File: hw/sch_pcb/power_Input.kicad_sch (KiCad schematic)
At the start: 40 parts, among them J1 USBC_USB4105-GF-A, J6 HEADER_2x01_PARALLEL, J7 HEADER_2x01_PARALLEL, J8 CONN1_1, J9 CONN1_1, Q1 DMTH3002LPS, U1 BQ25792RQMR1

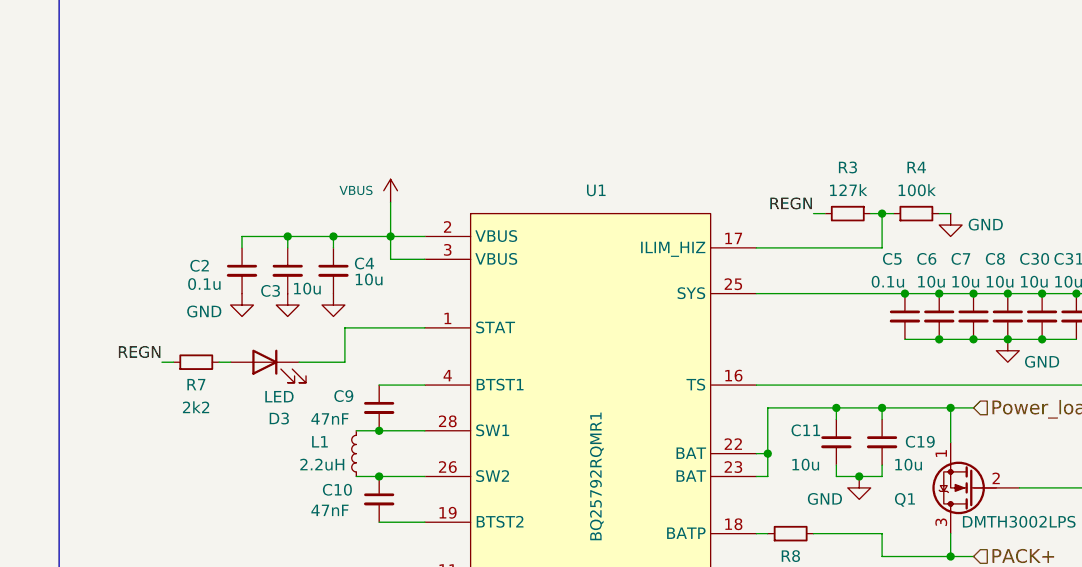
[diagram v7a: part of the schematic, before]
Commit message: Update USTids.
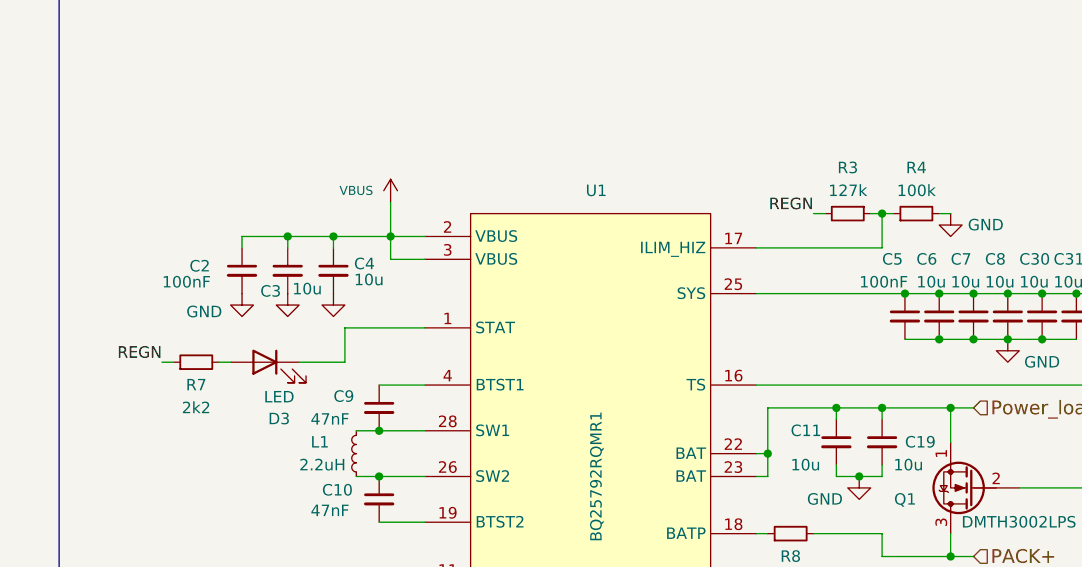
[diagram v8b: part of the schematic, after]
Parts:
- C10, C9: UST_ID (none) -> 65482046462c6d9e72056b98
- C11, C19, C25, C26, C27, C3, C30, C31, C4, C6, C7, C8: UST_ID (none) -> 5c70984712875079b91f8b53
- C2: value 0.1u -> 100nF; UST_ID (none) -> 5c70984712875079b91f8b4c
- C24: UST_ID (none) -> 5c70984812875079b91f8bf2
- C29: UST_ID 5c70984712875079b91f8b45 -> 5c70984712875079b91f8b4c
- C5: value 0.1u -> 100nF; UST_ID (none) -> 5c70984812875079b91f8bf2
- D3: UST_ID (none) -> 5c70984412875079b91f8892
- R11: UST_ID (none) -> 5c70984612875079b91f899f
- R3: UST_ID (none) -> 66a1559d6fdfe6f54e2ebeaa
- R4: UST_ID (none) -> 639ed3d540d28a66c9e88a9e
- R5: UST_ID (none) -> 66a159d36fdfe6f54e2ebef5
- R6: UST_ID (none) -> 66a15a4a6fdfe6f54e2ebf1b
- R7: UST_ID (none) -> 5c70984612875079b91f8990
- R8: UST_ID (none) -> 5c70984512875079b91f8977
- R9: UST_ID (none) -> 5c70984612875079b91f899c
- U1: UST_ID (none) -> 66a15cdb6fdfe6f54e2ebf66
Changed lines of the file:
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@@
 			)
 		)
+		(property "UST_ID" "66a1559d6fdfe6f54e2ebeaa"
+			(at 222.25 59.69 0)
+			(effects
+				(font
+					(size 1.27 1.27)
+				)
+				(hide yes)
+			)
+		)
 		(pin "1"
 		)
@@
 			)
 		)
+		(property "UST_ID" "5c70984712875079b91f8b53"
+			(at 247.65 71.12 0)
+			(effects
+				(font
+					(size 1.27 1.27)
+				)
+				(hide yes)
+			)
+		)
 		(pin "1"
 		)
@@
 			)
 		)
+		(property "UST_ID" "5c70984712875079b91f8b53"
+			(at 232.41 71.12 0)
+			(effects
+				(font
+					(size 1.27 1.27)
+				)
+				(hide yes)
+			)
+		)
 		(pin "1"
 		)
@@
 			)
 		)
+		(property "UST_ID" "5c70984412875079b91f8892"
+			(at 157.48 76.2 0)
+			(effects
+				(font
+					(size 1.27 1.27)
+				)
+				(hide yes)
+			)
+		)
 		(pin "1"
 		)
@@
 			)
 		)
+		(property "UST_ID" "5c70984712875079b91f8b53"
+			(at 160.02 66.04 0)
+			(effects
+				(font
+					(size 1.27 1.27)
+				)
+				(hide yes)
+			)
+		)
 		(pin "1"
 		)
@@
 			)
 		)
+		(property "UST_ID" "5c70984712875079b91f8b53"
+			(at 218.44 123.19 0)
+			(effects
+				(font
+					(size 1.27 1.27)
+				)
+				(hide yes)
+			)
+		)
 		(pin "1"
 		)
@@
 			)
 		)
-		(property "UST_ID" ""
+		(property "UST_ID" "5c70984612875079b91f899c"
 			(at 227.33 109.22 0)
 			(effects
@@
 			)
 		)
+		(property "UST_ID" "5c70984712875079b91f8b53"
+			(at 226.06 85.09 0)
+			(effects
+				(font
+					(size 1.27 1.27)
+				)
+				(hide yes)
+			)
+		)
 		(pin "1"
 		)
@@
 			)
 		)
+		(property "UST_ID" "66a15a4a6fdfe6f54e2ebf1b"
+			(at 256.54 82.55 0)
+			(effects
+				(font
+					(size 1.27 1.27)
+				)
+				(hide yes)
+			)
+		)
 		(pin "1"
 		)
@@
 			)
 		)
+		(property "UST_ID" "65482046462c6d9e72056b98"
+			(at 170.18 81.28 0)
+			(effects
+				(font
+					(size 1.27 1.27)
+				)
+				(hide yes)
+			)
+		)
 		(pin "1"
 		)
@@
 			)
 		)
-		(property "Value" "0.1u"
-			(at 224.79 67.31 0)
+		(property "Value" "100nF"
+			(at 223.52 67.31 0)
 			(effects
 				(font
@@
 			)
 		)
-		(property "UST_ID" ""
+		(property "UST_ID" "5c70984812875079b91f8bf2"
 			(at 228.6 71.12 0)
 			(effects
@@
 			)
 		)
+		(property "UST_ID" "5c70984712875079b91f8b53"
+			(at 228.6 123.19 0)
+			(effects
+				(font
+					(size 1.27 1.27)
+				)
+				(hide yes)
+			)
+		)
 		(pin "1"
 		)
@@
 			)
 		)
+		(property "UST_ID" "66a159d36fdfe6f54e2ebef5"
+			(at 256.54 74.93 0)
+			(effects
+				(font
+					(size 1.27 1.27)
+				)
+				(hide yes)
+			)
+		)
 		(pin "1"
 		)
@@
 			)
 		)
+		(property "UST_ID" "5c70984712875079b91f8b53"
+			(at 220.98 85.09 0)
+			(effects
+				(font
+					(size 1.27 1.27)
+				)
+				(hide yes)
+			)
+		)
 		(pin "1"
 		)
@@
 			)
 		)
+		(property "UST_ID" "5c70984612875079b91f899f"
+			(at 152.4 113.03 0)
+			(effects
+				(font
+					(size 1.27 1.27)
+				)
+				(hide yes)
+			)
+		)
 		(pin "1"
 		)
@@
 			)
 		)
+		(property "UST_ID" "5c70984712875079b91f8b53"
+			(at 223.52 123.19 0)
+			(effects
+				(font
+					(size 1.27 1.27)
+				)
+				(hide yes)
+			)
+		)
 		(pin "1"
 		)
@@
 			)
 		)
-		(property "UST_ID" ""
+		(property "UST_ID" "65482046462c6d9e72056b98"
 			(at 170.18 91.44 0)
 			(effects
@@
 			)
 		)
-		(property "UST_ID" ""
+		(property "UST_ID" "66a15cdb6fdfe6f54e2ebf66"
 			(at 193.04 59.69 0)
 			(effects
@@
 			)
 		)
-		(property "UST_ID" ""
+		(property "UST_ID" "5c70984512875079b91f8977"
 			(at 215.9 95.25 0)
 			(effects
@@
 			)
 		)
+		(property "UST_ID" "639ed3d540d28a66c9e88a9e"
+			(at 229.87 59.69 0)
+			(effects
+				(font
+					(size 1.27 1.27)
+				)
+				(hide yes)
+			)
+		)
 		(pin "1"
 		)
@@
 			)
 		)
-		(property "Value" "0.1u"
-			(at 148.844 67.564 0)
+		(property "Value" "100nF"
+			(at 146.05 67.31 0)
 			(effects
 				(font
@@
 			)
 		)
+		(property "UST_ID" " 5c70984712875079b91f8b4c"
+			(at 154.94 66.04 0)
+			(effects
+				(font
+					(size 1.27 1.27)
+				)
+				(hide yes)
+			)
+		)
 		(pin "1"
 		)
@@
 			)
 		)
-		(property "UST_ID" ""
+		(property "UST_ID" "5c70984812875079b91f8bf2"
 			(at 213.36 123.19 0)
 			(effects
@@
 			)
 		)
+		(property "UST_ID" "5c70984712875079b91f8b53"
+			(at 240.03 71.12 0)
+			(effects
+				(font
+					(size 1.27 1.27)
+				)
+				(hide yes)
+			)
+		)
 		(pin "1"
 		)
@@
 			)
 		)
+		(property "UST_ID" "5c70984712875079b91f8b53"
+			(at 165.1 66.04 0)
+			(effects
+				(font
+					(size 1.27 1.27)
+				)
+				(hide yes)
+			)
+		)
 		(pin "1"
 		)
@@
 			)
 		)
-		(property "UST_ID" ""
+		(property "UST_ID" "5c70984612875079b91f8990"
 			(at 149.86 76.2 0)
 			(effects
@@
 			)
 		)
+		(property "UST_ID" "5c70984712875079b91f8b53"
+			(at 243.84 71.12 0)
+			(effects
+				(font
+					(size 1.27 1.27)
+				)
+				(hide yes)
+			)
+		)
 		(pin "1"
 		)
@@
 			)
 		)
+		(property "UST_ID" "5c70984712875079b91f8b53"
+			(at 236.22 71.12 0)
+			(effects
+				(font
+					(size 1.27 1.27)
+				)
+				(hide yes)
+			)
+		)
 		(pin "1"
 		)
@@
 			)
 		)
-		(property "UST_ID" "5c70984712875079b91f8b45"
+		(property "UST_ID" " 5c70984712875079b91f8b4c "
 			(at 49.53 144.78 0)
 			(effects
